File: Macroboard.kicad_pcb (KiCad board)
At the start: 2 copper layers, 34 parts, among them SW1 SW_Push, U1 ATmega32U4-AU, Y1 16MHz

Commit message: PCB v1 done
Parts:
- added G***: LOGO, Macroboard:JM_logo, F.Cu at (261.1, 69.1)
- moved C6 35.8 mm to (256.4, 80.9), turned to 270 degrees
- moved C4 35.1 mm to (254.4, 68.2), turned to 90 degrees
- moved R3 18.4 mm to (220.1, 75.4), turned to 90 degrees
- moved R2 14.4 mm to (223.4, 75.4), turned to 90 degrees
- moved C7 11.1 mm to (231.9, 75.4), turned to 90 degrees
- moved C5 8.91 mm to (227.5, 75.4), turned to 90 degrees
- moved R1 7.34 mm to (237.5, 69.2), turned to 90 degrees
- moved C3 3.56 mm to (236.6, 75.6), turned to 270 degrees
- moved SW1 3.33 mm to (231.8, 68.3), turned to 180 degrees
- moved F1 1.15 mm to (216.4, 75.8)
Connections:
- U1 pad 36: Net-(U1-Pad36) -> COL2
- U1 pad 37: Net-(U1-Pad37) -> COL1
- U1 pad 38: Net-(U1-Pad38) -> COL0
- U1 pad 39: Net-(U1-Pad39) -> ROW2
- U1 pad 40: Net-(U1-Pad40) -> ROW1
- U1 pad 41: Net-(U1-Pad41) -> ROW0
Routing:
- net ROW2: track 0.00 -> 140.8 mm
- net ROW1: track 0.00 -> 124.1 mm, vias 0 -> 2
- net COL0: track 0.00 -> 75.6 mm
- net ROW0: track 0.00 -> 71.1 mm, vias 0 -> 2
- net COL1: track 0.00 -> 57.4 mm
- net COL2: track 0.00 -> 49.3 mm
- net D-: track 26.4 -> 4.84 mm
- net Net-(R3-Pad1): track 5.17 -> 24.0 mm
- net D+: track 23.3 -> 5.48 mm
- net Net-(R2-Pad1): track 5.07 -> 22.6 mm
- net +5V: track 90.5 -> 107.2 mm, vias 4 -> 10
- net GND: track 111.2 -> 98.2 mm, vias 2 -> 0
- net VCC: track 5.14 -> 14.4 mm
- net Net-(D8-Pad2): track 0.00 -> 6.82 mm
- net Net-(D7-Pad2): track 0.00 -> 6.82 mm
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- added copper zone on B.Cu, net GND
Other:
- board outline added: 57.2 x 81.8 mm

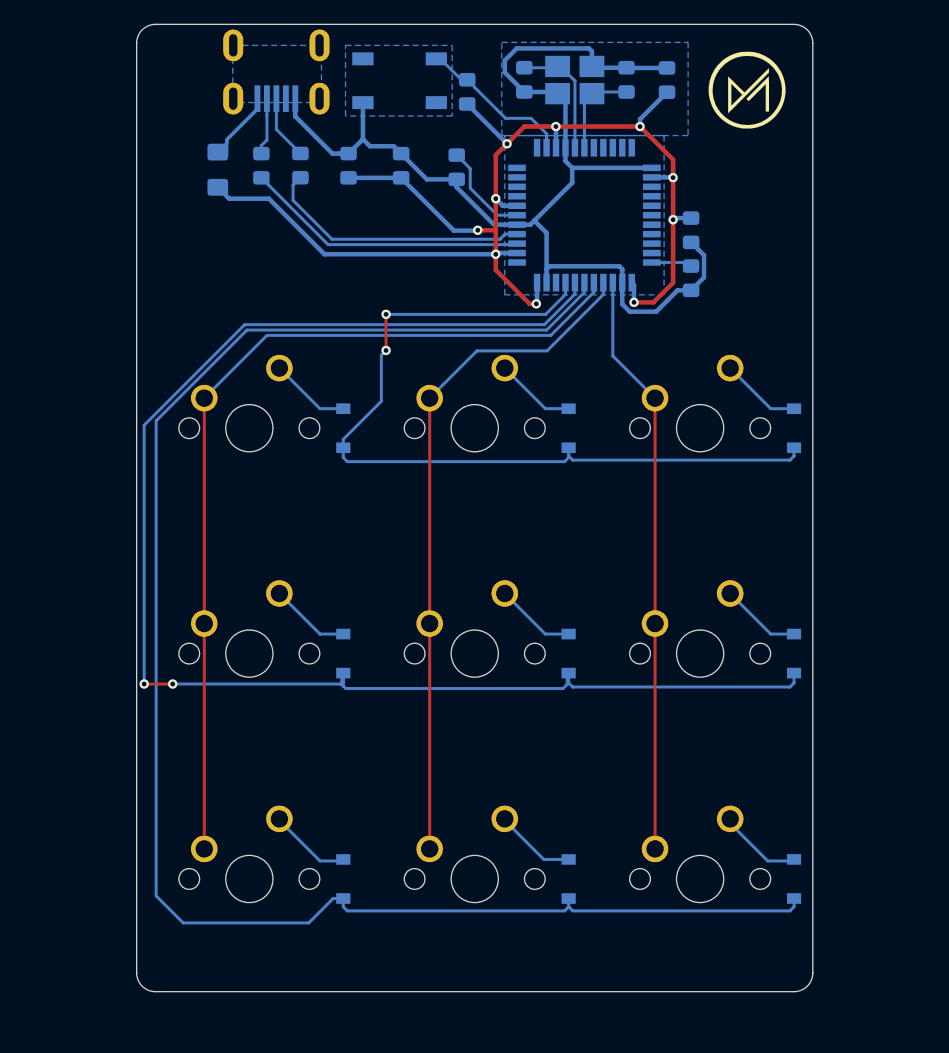
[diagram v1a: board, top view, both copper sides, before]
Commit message: mounting holes to PCB
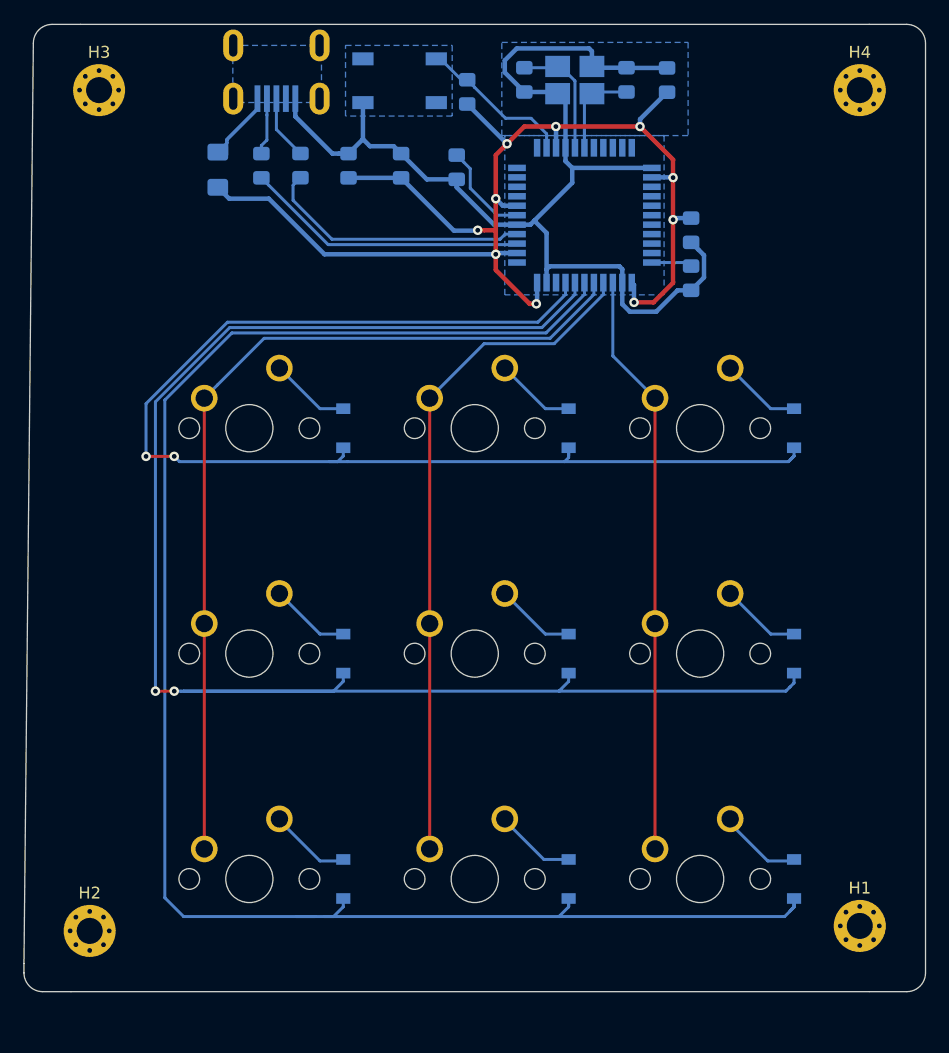
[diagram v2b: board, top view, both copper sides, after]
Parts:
- removed G***: LOGO, Macroboard:JM_logo
- added H1: MountingHole, MountingHole:MountingHole_2.2mm_M2_Pad_Via, F.Cu at (270.7, 139.7)
- added H2: MountingHole, MountingHole:MountingHole_2.2mm_M2_Pad_Via, F.Cu at (205.6, 140.1)
- added H3: MountingHole, MountingHole:MountingHole_2.2mm_M2_Pad_Via, F.Cu at (206.4, 69.1)
- added H4: MountingHole, MountingHole:MountingHole_2.2mm_M2_Pad_Via, F.Cu at (270.7, 69.1)
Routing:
- net ROW0: track 71.1 -> 105.0 mm
- net ROW1: track 124.1 -> 136.0 mm
- net ROW2: track 140.8 -> 145.1 mm
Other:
- board size 57.2 x 81.8 mm -> 76.2 x 81.8 mm

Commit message: LED-switches added
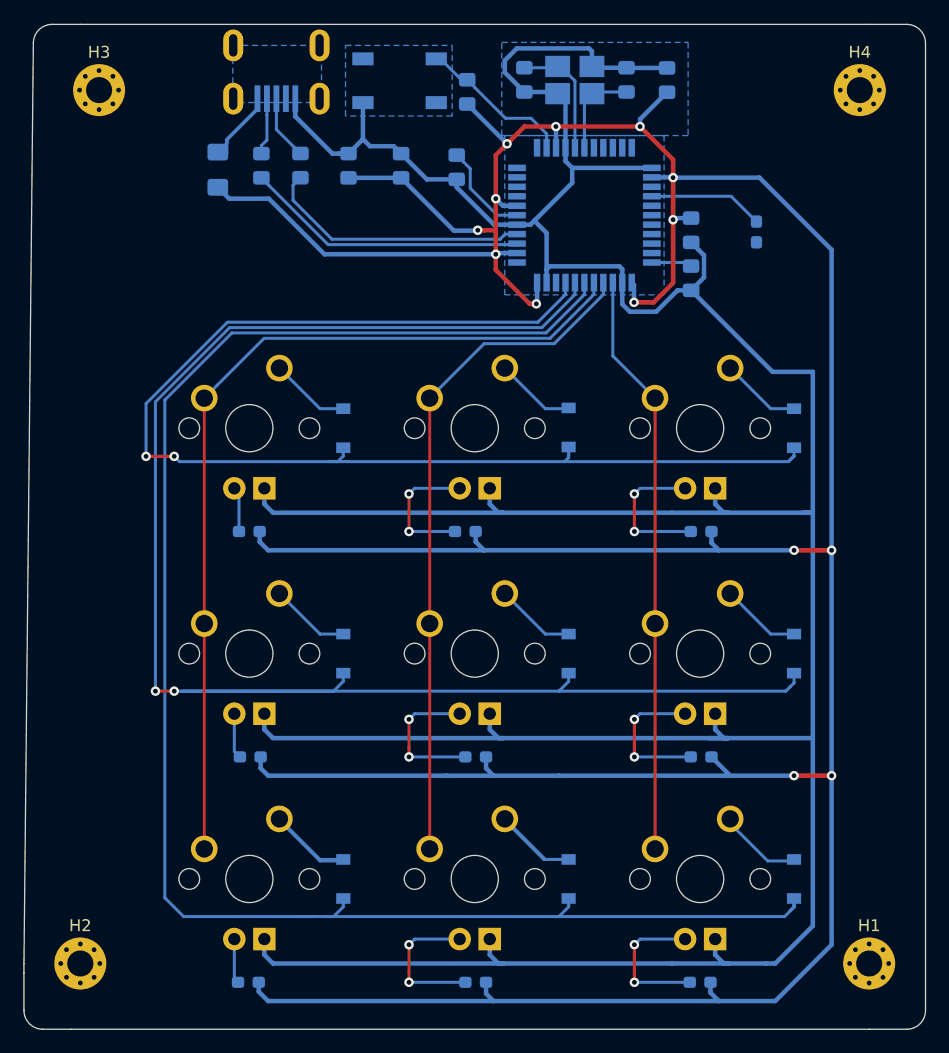
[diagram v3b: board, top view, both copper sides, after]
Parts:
- removed D1, D2, D3, D4, D5, D6, D7, D8, D9: D_Small, Diode_SMD:D_SOD-123
- added D10: D_Small, Diode_SMD:D_SOD-123, B.Cu at (227.0, 97.6)
- added D11: D_Small, Diode_SMD:D_SOD-123, B.Cu at (246.1, 97.6)
- added D12: D_Small, Diode_SMD:D_SOD-123, B.Cu at (265.1, 97.6)
- added D13: D_Small, Diode_SMD:D_SOD-123, B.Cu at (227.0, 116.7)
- added D14: D_Small, Diode_SMD:D_SOD-123, B.Cu at (246.1, 116.7)
- added D15: D_Small, Diode_SMD:D_SOD-123, B.Cu at (265.1, 116.7)
- added D16: D_Small, Diode_SMD:D_SOD-123, B.Cu at (227.0, 135.7)
- added D17: D_Small, Diode_SMD:D_SOD-123, B.Cu at (246.1, 135.7)
- added D18: D_Small, Diode_SMD:D_SOD-123, B.Cu at (265.1, 135.7)
- added R10: 200, Resistor_SMD:R_0603_1608Metric_Pad1.05x0.95mm_HandSolder, B.Cu at (257.3, 125.4)
- added R11: 200, Resistor_SMD:R_0603_1608Metric_Pad1.05x0.95mm_HandSolder, B.Cu at (219.0, 144.5)
- added R12: 200, Resistor_SMD:R_0603_1608Metric_Pad1.05x0.95mm_HandSolder, B.Cu at (238.2, 144.5)
- added R13: 200, Resistor_SMD:R_0603_1608Metric_Pad1.05x0.95mm_HandSolder, B.Cu at (257.2, 144.5)
- added R14: R_Small, Resistor_SMD:R_0603_1608Metric_Pad1.05x0.95mm_HandSolder, B.Cu at (261.9, 81.0)
- added R5: 200, Resistor_SMD:R_0603_1608Metric_Pad1.05x0.95mm_HandSolder, B.Cu at (219.1, 106.4)
- added R6: 200, Resistor_SMD:R_0603_1608Metric_Pad1.05x0.95mm_HandSolder, B.Cu at (237.3, 106.4)
- added R7: 200, Resistor_SMD:R_0603_1608Metric_Pad1.05x0.95mm_HandSolder, B.Cu at (257.3, 106.4)
- added R8: 200, Resistor_SMD:R_0603_1608Metric_Pad1.05x0.95mm_HandSolder, B.Cu at (219.2, 125.4)
- added R9: 200, Resistor_SMD:R_0603_1608Metric_Pad1.05x0.95mm_HandSolder, B.Cu at (238.2, 125.4)
- MX1, MX2, MX3, MX4, MX5, MX6, MX7, MX8, MX9: value MX-NoLED -> MX-LED; footprint MX_Only:MXOnly-1U-NoLED -> MX_Only:MXOnly-1U
- moved H1 3.27 mm to (271.5, 142.9)
- moved H2 2.87 mm to (204.8, 142.9)
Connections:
- MX2 pad 1: COL1 -> Net-(MX2-Pad1)
- MX3 pad 1: COL2 -> Net-(MX3-Pad1)
- MX4 pad 1: COL0 -> Net-(MX4-Pad1)
- MX5 pad 1: COL1 -> Net-(MX5-Pad1)
- MX6 pad 1: COL2 -> Net-(MX6-Pad1)
- MX7 pad 1: COL0 -> Net-(MX7-Pad1)
- U1 pad 26: Net-(U1-Pad26) -> LEDS
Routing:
- net +5V: track 107.2 -> 343.9 mm, vias 10 -> 14
- net GND: track 98.2 -> 322.4 mm
- net Net-(MX9-Pad3): track 0.00 -> 12.4 mm, vias 0 -> 2
- net Net-(MX8-Pad3): track 0.00 -> 12.4 mm, vias 0 -> 2
- net Net-(MX6-Pad3): track 0.00 -> 12.4 mm, vias 0 -> 2
- net Net-(MX5-Pad3): track 0.00 -> 12.4 mm, vias 0 -> 2
- net Net-(MX3-Pad3): track 0.00 -> 12.4 mm, vias 0 -> 2
- net Net-(MX2-Pad3): track 0.00 -> 11.5 mm, vias 0 -> 2
- net LEDS: track 0.00 -> 9.73 mm
- net Net-(D17-Pad2): track 6.82 -> 13.6 mm
- net Net-(D16-Pad2): track 6.82 -> 13.6 mm
- net Net-(MX4-Pad3): track 0.00 -> 3.85 mm
- net Net-(MX1-Pad3): track 0.00 -> 3.81 mm
- net Net-(MX7-Pad3): track 0.00 -> 3.78 mm
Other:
- board size 76.2 x 81.8 mm -> 76.2 x 84.9 mm

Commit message: added fet
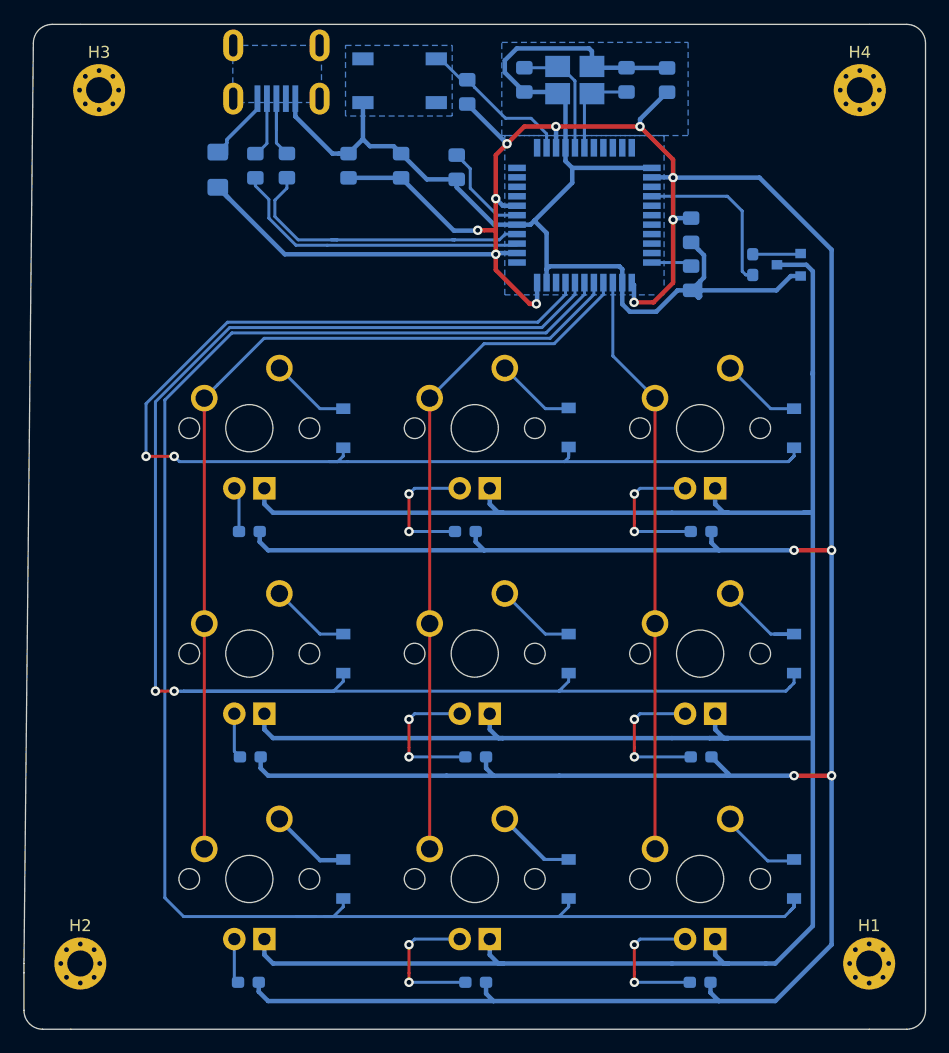
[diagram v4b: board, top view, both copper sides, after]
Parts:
- added Q1: 2N7002, Package_TO_SOT_SMD:SOT-23, B.Cu at (264.7, 83.8)
- R10, R11, R12, R13, R5, R6, R7, R8, R9: value 200 -> 220
- R14: value R_Small -> 1k
- moved R14 2.78 mm to (261.6, 83.8), turned to 270 degrees
- moved R2 1.14 mm to (222.2, 75.4)
- moved R3 0.51 mm to (219.6, 75.4)
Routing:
- net Net-(MX1-Pad4): track 0.00 -> 240.0 mm
- net GND: track 322.4 -> 110.3 mm
- net LEDS: track 9.73 -> 14.3 mm
- net Net-(Q1-Pad1): track 0.00 -> 4.07 mm
- net Net-(R2-Pad1): track 22.6 -> 25.9 mm
- net D+: track 5.48 -> 7.61 mm
- net Net-(R3-Pad1): track 24.0 -> 25.8 mm
- net Net-(D15-Pad2): track 6.82 -> 8.50 mm
- net +5V: track 343.9 -> 345.3 mm
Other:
- net class LED_pwr added: clearance 0.2, trace_width 0.381, via_dia 0.8, via_drill 0.4

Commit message: new button and hotfixin
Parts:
- SW1: footprint random-keyboard-parts:SKQG-1155865 -> Button_Switch_THT:SW_PUSH_6mm_H4.3mm
- moved SW1 4.31 mm to (228.3, 70.9), turned to 0 degrees
- moved R1 1.31 mm to (238.6, 69.8)
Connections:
- net Net-(MX1-Pad3) renamed L_MX1
- net Net-(MX1-Pad4) renamed LED_TRN
- net Net-(MX2-Pad3) renamed L_MX2
- net Net-(MX3-Pad3) renamed L_MX3
- net Net-(MX4-Pad3) renamed L_MX4
- net Net-(MX5-Pad3) renamed L_MX5
- net Net-(MX6-Pad3) renamed L_MX6
- net Net-(MX7-Pad3) renamed L_MX7
- net Net-(MX8-Pad3) renamed L_MX8
- net Net-(MX9-Pad3) renamed L_MX9
- MX2 pad 1: Net-(MX2-Pad1) -> COL1
- MX3 pad 1: Net-(MX3-Pad1) -> COL2
- MX4 pad 1: Net-(MX4-Pad1) -> COL0
- MX5 pad 1: Net-(MX5-Pad1) -> COL1
- MX6 pad 1: Net-(MX6-Pad1) -> COL2
- MX7 pad 1: Net-(MX7-Pad1) -> COL0
- USB1 pad 6: Net-(USB1-Pad6) -> GND
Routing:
- net LED_TRN: track 240.0 -> 223.4 mm
- net Net-(R1-Pad2): track 13.1 -> 20.3 mm
- net GND: track 110.3 -> 115.2 mm
- net COL2: track 49.3 -> 46.2 mm
- net COL1: track 57.4 -> 54.2 mm
- net +5V: track 345.3 -> 344.1 mm
